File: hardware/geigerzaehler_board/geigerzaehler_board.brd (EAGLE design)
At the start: 100 x 80 mm, 24 parts, among them IC1 IRFDC20, IC2 MC34063AP, IC3 40106N, Q1 BC327, X1 GMSTBV2

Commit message: completed first version of geigerzähler-board
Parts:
- removed X1: GMSTBV2, con-phoenix-762:GMSTBV2
- added C14: 100n, rcl:C050-025X075
- added C2: 22p, rcl:C025-025X050
- added C7: 10n, rcl:C050-025X075
- added CT+, CT-: TPSQPAD1-13Y, testpad:P1-13Y
- added Q5: BC327, transistor-pnp:TO92
- added R11: 470k, rcl:0207/10
- added R6: 560k, rcl:0207/10
- added R7, R8: 1k5, rcl:0207/10
- added TP2: TPPAD1-13Y, testpad:P1-13Y
- D2: value 1N4148DO35-7 -> 1N4148; device diode:DO35-7 -> diode:DO35-10
- Q1: value BC327 -> BC547; device transistor-pnp:TO92 -> transistor:TO92
- moved Q1 49.6 mm to (65.4, 44.5), turned to 90 degrees
- moved D2 29.2 mm to (76.8, 28.6)
- moved IC3 20.3 mm to (78.1, 40.6), turned to 90 degrees
- moved JP1 5.12 mm to (47.6, 20.3), turned to 0 degrees
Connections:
- removed net N$10: IC3.4, IC3.5
- new net N$13: C2.1, CT-.TP, R7.1
- new net N$14: Q1.2, R6.2, R7.2
- new net N$15: D2.C, Q1.3, R8.1
- new net N$16: C7.1, D2.A, IC3.1, R11.1
- net GND: now also C14.2, C2.2, C7.2, IC3.3, IC3.5, Q1.1, Q5.3, R6.1; no longer Q1.3
- net N$1: now also Q5.2; no longer Q1.2
- net N$12: now also CT+.TP
- net N$2: now also Q5.1; no longer Q1.1
- net PULSE: now also IC3.2, TP2.TP; no longer IC3.6
- net VCC: now also C14.1, R11.2, R8.2
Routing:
- net GND: track 147.0 -> 262.1 mm
- net PULSE: track 0.00 -> 45.3 mm
- net VCC: track 0.00 -> 43.5 mm
- net N$15: track 0.00 -> 18.3 mm
- net N$14: track 0.00 -> 12.4 mm
- net N$16: track 0.00 -> 11.4 mm
- net N$13: track 0.00 -> 7.62 mm
- net N$12: track 0.00 -> 3.81 mm
- net VBAT: track 54.2 -> 52.3 mm

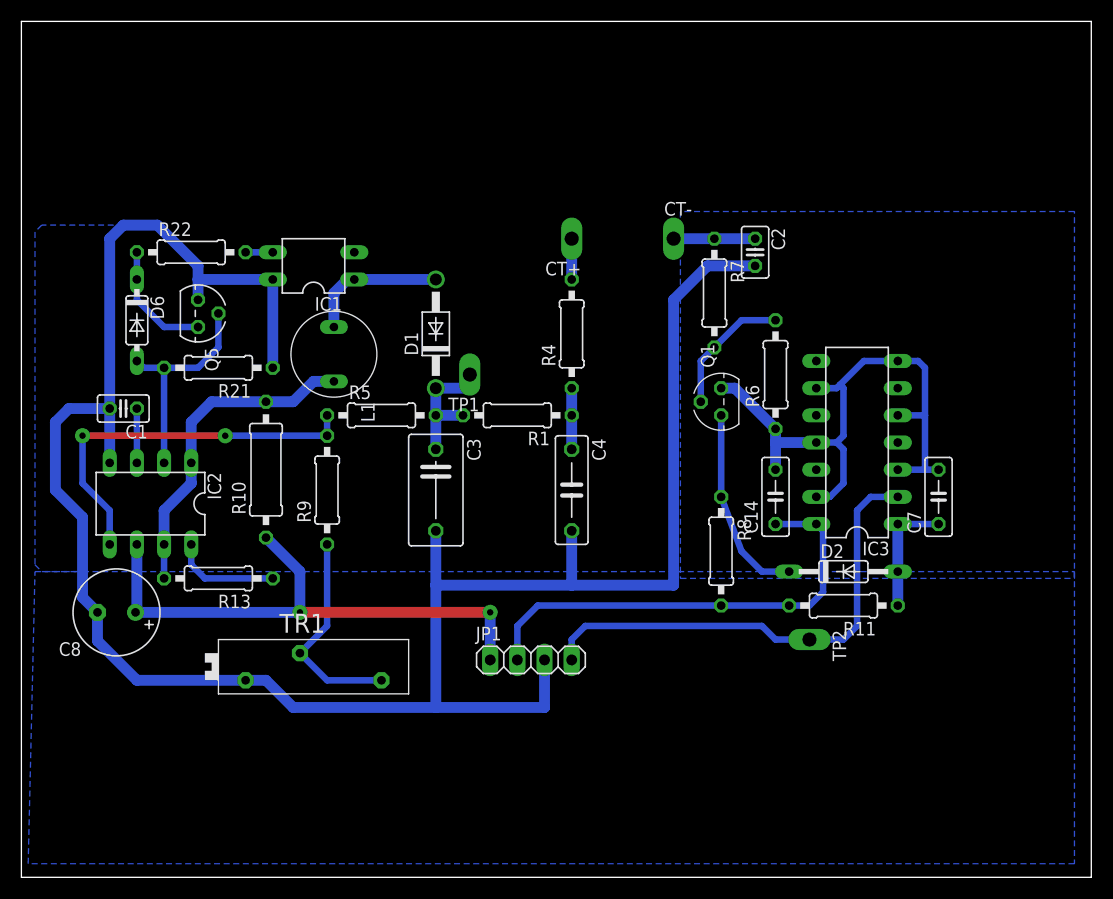
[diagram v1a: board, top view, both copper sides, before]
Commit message: optimized geigerzähler-board
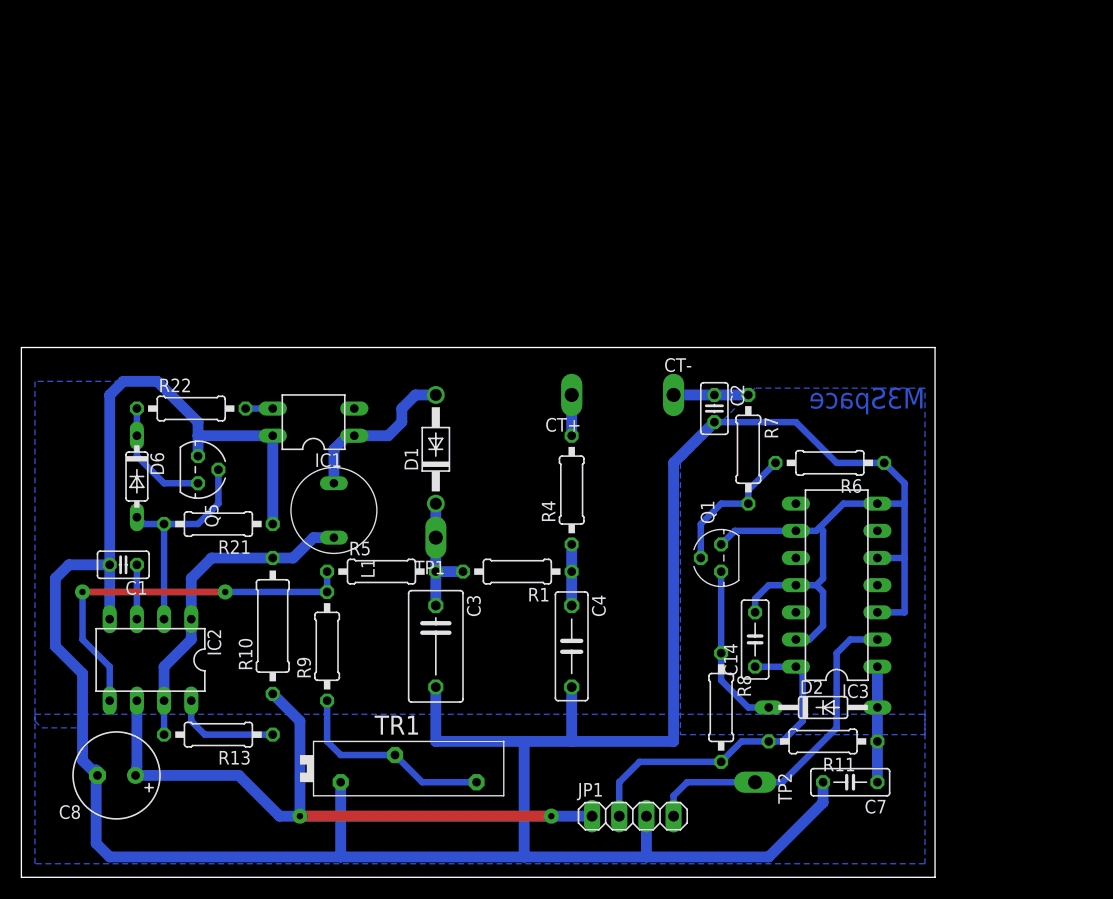
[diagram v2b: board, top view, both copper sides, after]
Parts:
- moved C7 27.9 mm to (77.5, 8.89), turned to 180 degrees
- moved JP1 17.4 mm to (57.1, 5.71)
- moved TP1 15.6 mm to (38.7, 31.8)
- moved C8 15.2 mm to (8.89, 9.53)
- moved C2 15.1 mm to (64.8, 43.8)
- moved R7 14.9 mm to (67.9, 40.0)
- moved R10 14.6 mm to (23.5, 23.5)
- moved L1 14.6 mm to (29.2, 34.3)
- moved Q1 14.6 mm to (65.4, 29.8)
- moved R22 14.6 mm to (15.9, 43.8)
- moved C3 14.6 mm to (38.7, 21.6)
- moved C4 14.6 mm to (51.4, 21.6)
- moved R1 14.6 mm to (46.4, 28.6)
- moved R13 14.6 mm to (18.4, 13.3)
- moved R5 14.6 mm to (33.7, 28.6)
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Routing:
- net GND: track 262.1 -> 317.1 mm
- net PULSE: track 45.3 -> 31.1 mm
- net VCC: track 43.5 -> 31.8 mm
- net VBAT: track 52.3 -> 63.7 mm
- net N$15: track 18.3 -> 15.7 mm
- net N$4: track 13.2 -> 15.5 mm
- net N$14: track 12.4 -> 13.3 mm
- net N$13: track 7.62 -> 6.98 mm
- net VHIGH: track 12.7 -> 12.1 mm
- net N$16: track 11.4 -> 10.8 mm
- net N$9: track 19.9 -> 19.4 mm
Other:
- board size 100 x 80 mm -> 85.4 x 49.5 mm
- board text added: "M3Space"
